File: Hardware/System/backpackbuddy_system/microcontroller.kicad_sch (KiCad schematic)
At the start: 10 parts, among them SW2 MCU RESET, U1 ATmega32U4-A, Y1 16MHz

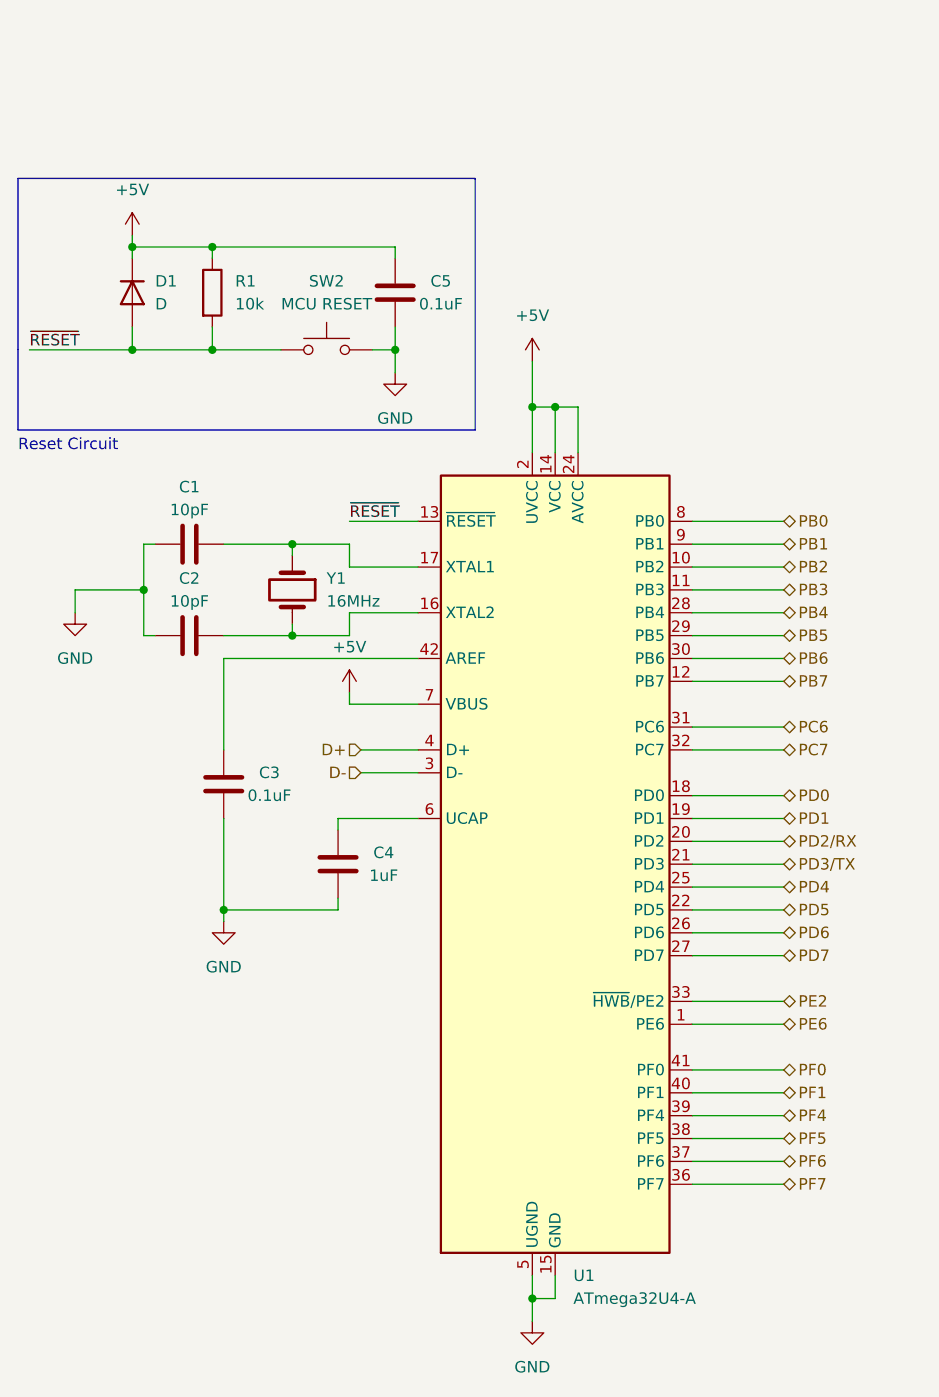
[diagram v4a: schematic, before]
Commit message: schematic mostly done, just need to fix ERC, decoup caps, TP
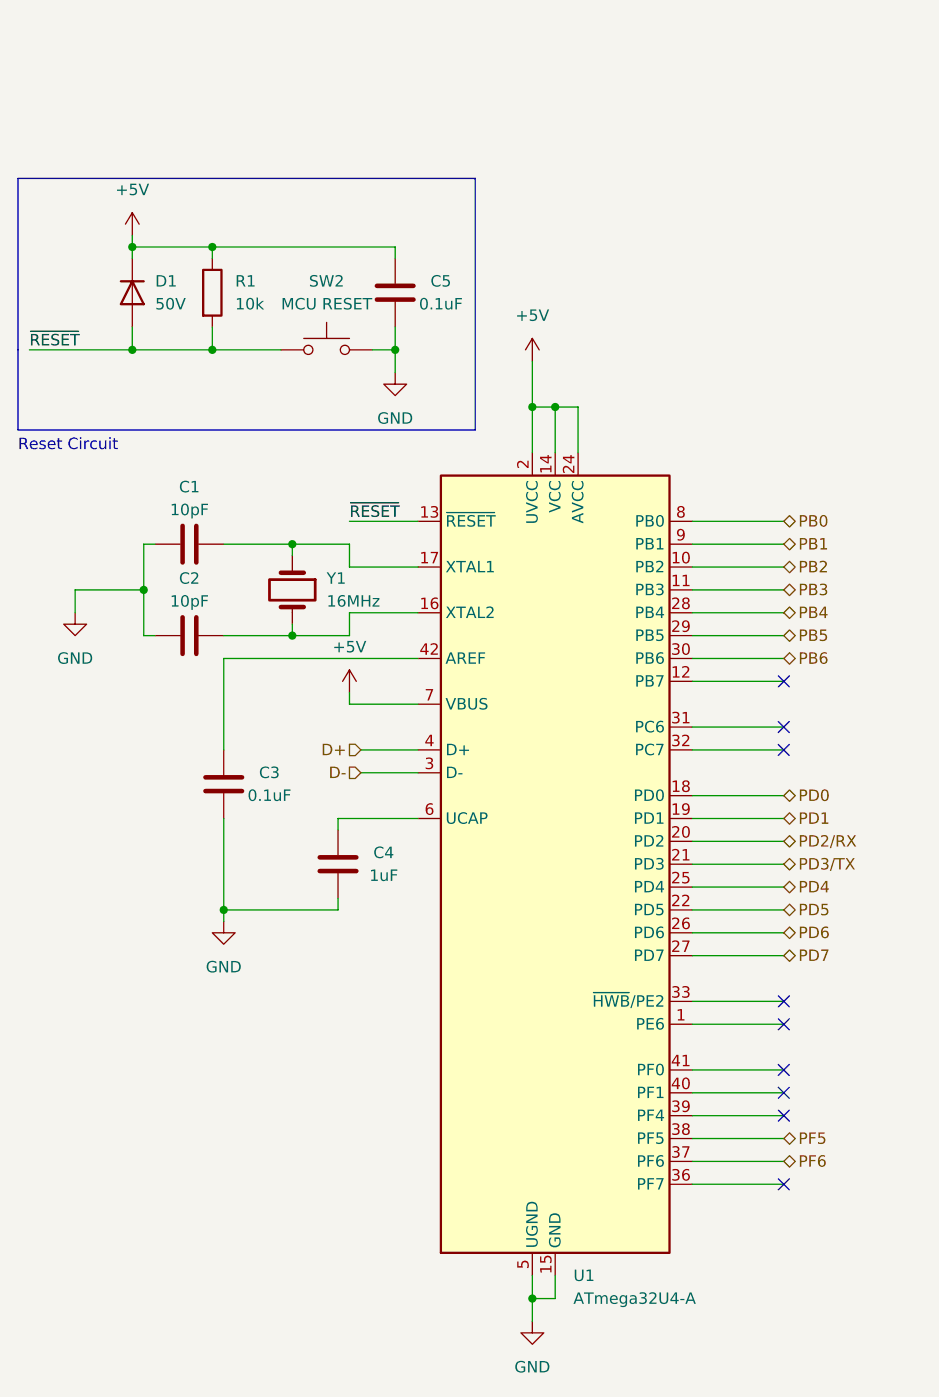
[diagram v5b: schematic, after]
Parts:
- D1: value D -> 50V; footprint (none) -> Diode_SMD:D_SMB_Handsoldering; MPN (none) -> DIODE SCHOTTKY 50V 1A SMB; Stock (none) -> https://www.digikey.com/en/products/detail/diodes-incorpora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
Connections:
- net PB7: no longer names the net of U1.12 (PB7)
- net PC6: no longer names the net of U1.31 (PC6)
- net PC7: no longer names the net of U1.32 (PC7)
- net PE2: no longer names the net of U1.33 (~{HWB}/PE2)
- net PE6: no longer names the net of U1.1 (PE6)
- net PF0: no longer names the net of U1.41 (PF0)
- net PF1: no longer names the net of U1.40 (PF1)
- net PF4: no longer names the net of U1.39 (PF4)
- net PF7: no longer names the net of U1.36 (PF7)
- no-connect marks 0 -> 9
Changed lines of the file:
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@@
   (junction (at 147.32 58.42) (diameter 0) (color 0 0 0 0)
   )
+  (no_connect (at 172.72 134.62))
+  (no_connect (at 172.72 88.9))
+  (no_connect (at 172.72 144.78))
+  (no_connect (at 172.72 124.46))
+  (no_connect (at 172.72 93.98))
+  (no_connect (at 172.72 132.08))
+  (no_connect (at 172.72 127))
+  (no_connect (at 172.72 137.16))
+  (no_connect (at 172.72 96.52))
   (wire (pts (xy 100.33 40.64) (xy 100.33 41.91))
     (stroke (width 0) (type default) (color 0 0 0 0))
@@
     (effects (font (size 1.27 1.27)) (justify left bottom))
   )
-  (hierarchical_label "PC6" (shape bidirectional) (at 172.72 93.98 0)
-    (effects (font (size 1.27 1.27)) (justify left))
-  )
   (hierarchical_label "PD1" (shape bidirectional) (at 172.72 104.14 0)
     (effects (font (size 1.27 1.27)) (justify left))
@@
     (effects (font (size 1.27 1.27)) (justify left))
   )
-  (hierarchical_label "PB7" (shape bidirectional) (at 172.72 88.9 0)
-    (effects (font (size 1.27 1.27)) (justify left))
-  )
   (hierarchical_label "PD6" (shape bidirectional) (at 172.72 116.84 0)
     (effects (font (size 1.27 1.27)) (justify left))
@@
     (effects (font (size 1.27 1.27)) (justify left))
   )
-  (hierarchical_label "PF1" (shape bidirectional) (at 172.72 134.62 0)
-    (effects (font (size 1.27 1.27)) (justify left))
-  )
   (hierarchical_label "PD7" (shape bidirectional) (at 172.72 119.38 0)
     (effects (font (size 1.27 1.27)) (justify left))
@@
     (effects (font (size 1.27 1.27)) (justify left))
   )
-  (hierarchical_label "PF0" (shape bidirectional) (at 172.72 132.08 0)
-    (effects (font (size 1.27 1.27)) (justify left))
-  )
   (hierarchical_label "PB0" (shape bidirectional) (at 172.72 71.12 0)
     (effects (font (size 1.27 1.27)) (justify left))
@@
     (effects (font (size 1.27 1.27)) (justify left))
   )
-  (hierarchical_label "PF4" (shape bidirectional) (at 172.72 137.16 0)
-    (effects (font (size 1.27 1.27)) (justify left))
-  )
   (hierarchical_label "PB5" (shape bidirectional) (at 172.72 83.82 0)
     (effects (font (size 1.27 1.27)) (justify left))
@@
   )
   (hierarchical_label "PB3" (shape bidirectional) (at 172.72 78.74 0)
-    (effects (font (size 1.27 1.27)) (justify left))
-  )
-  (hierarchical_label "PC7" (shape bidirectional) (at 172.72 96.52 0)
-    (effects (font (size 1.27 1.27)) (justify left))
-  )
-  (hierarchical_label "PE6" (shape bidirectional) (at 172.72 127 0)
-    (effects (font (size 1.27 1.27)) (justify left))
-  )
-  (hierarchical_label "PF7" (shape bidirectional) (at 172.72 144.78 0)
     (effects (font (size 1.27 1.27)) (justify left))
   )
@@
   )
   (hierarchical_label "PD3{slash}TX" (shape bidirectional) (at 172.72 109.22 0)
-    (effects (font (size 1.27 1.27)) (justify left))
-  )
-  (hierarchical_label "PE2" (shape bidirectional) (at 172.72 124.46 0)
     (effects (font (size 1.27 1.27)) (justify left))
   )
@@
       (effects (font (size 1.27 1.27)) (justify left))
     )
-    (property "Value" "D" (id 1) (at 102.87 46.9899 90)
+    (property "Value" "50V" (id 1) (at 102.87 46.9899 90)
       (effects (font (size 1.27 1.27)) (justify left))
     )
-    (property "Footprint" "" (id 2) (at 100.33 45.72 0)
+    (property "Footprint" "Diode_SMD:D_SMB_Handsoldering" (id 2) (at 100.33 45.72 0)
       (effects (font (size 1.27 1.27)) hide)
     )
@@
       (effects (font (size 1.27 1.27)) hide)
     )
+    (property "MPN" "DIODE SCHOTTKY 50V 1A SMB" (id 4) (at 100.33 45.72 0)
+      (effects (font (size 1.27 1.27)) hide)
+    )
+    (property "Stock" "https://www.digikey.com/en/products/detail/diodes-incorporated/B150B-13-F/775856?utm_adgroup=General&utm_source=google&utm_medium=cpc&utm_campaign=PMax%20Shopping_Product_Zombie%20SKUs&utm_term=&utm_content=General" (id 5) (at 100.33 45.72 0)
+      (effects (font (size 1.27 1.27)) hide)
+    )

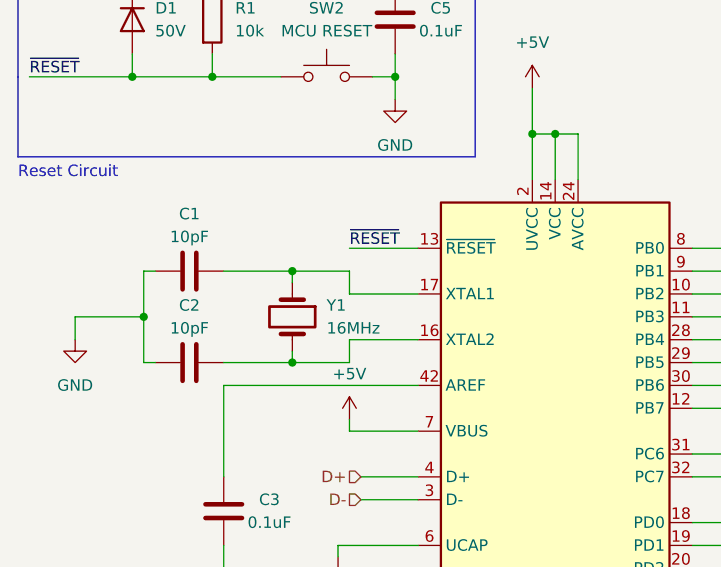
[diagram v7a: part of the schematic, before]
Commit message: fixed lm3940 symbol, changed crystal stuff
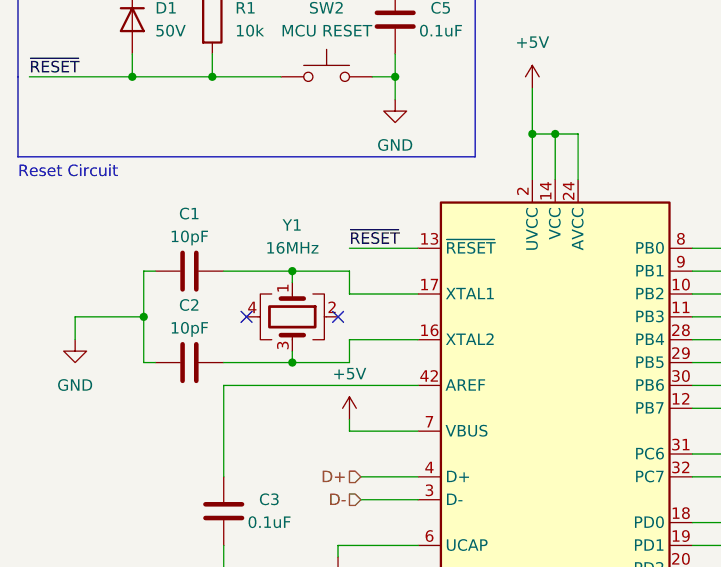
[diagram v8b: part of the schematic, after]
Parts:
- removed Y1: 16MHz, Crystal:Crystal_SMD_3225-4Pin_3.2x2.5mm_HandSoldering, symbol Device:Crystal
- added Y1: 16MHz, Crystal:Crystal_SMD_3225-4Pin_3.2x2.5mm_HandSoldering, symbol Device:Crystal_GND24
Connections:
- net at C1.2, U1.17 (XTAL1): now also Y1.1
- net at C2.2, U1.16 (XTAL2): now also Y1.3
- no-connect marks 9 -> 11
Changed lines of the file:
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@@
   (no_connect (at 172.72 124.46))
   (no_connect (at 172.72 93.98))
+  (no_connect (at 113.03 78.74))
   (no_connect (at 172.72 132.08))
   (no_connect (at 172.72 127))
+  (no_connect (at 123.19 78.74))
   (no_connect (at 172.72 137.16))
   (no_connect (at 172.72 96.52))
@@
     (pin "1")
   )
-  (symbol (lib_id "Device:Crystal") (at 118.11 78.74 270) (unit 1)
-    (in_bom yes) (on_board yes) (fields_autoplaced)
-    (property "Reference" "Y1" (id 0) (at 121.92 77.4699 90)
-      (effects (font (size 1.27 1.27)) (justify left))
-    )
-    (property "Value" "16MHz" (id 1) (at 121.92 80.0099 90)
-      (effects (font (size 1.27 1.27)) (justify left))
-    )
+  (symbol (lib_id "Device:Crystal_GND24") (at 118.11 78.74 270) (unit 1)
+    (in_bom yes) (on_board yes)
+    (property "Reference" "Y1" (id 0) (at 118.11 68.58 90))
+    (property "Value" "16MHz" (id 1) (at 118.11 71.12 90))
     (property "Footprint" "Crystal:Crystal_SMD_3225-4Pin_3.2x2.5mm_HandSoldering" (id 2) (at 118.11 78.74 0)
       (effects (font (size 1.27 1.27)) hide)
@@
     (pin "1")
     (pin "2")
+    (pin "3")
+    (pin "4")
   )
   (symbol (lib_id "Device:C") (at 123.19 109.22 0) (unit 1)
